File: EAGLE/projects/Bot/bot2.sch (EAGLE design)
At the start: 20 parts, among them IC1 7805T, U3 ARDUINO_SHIELDLABEL

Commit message: PCB Updates
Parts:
- removed S1: (no value), switch1:MS243
- added S2: (no value), switch2:MS243
- IC1: value 7805T -> (none); device linear:7805T -> linearMe:7905T
- LED1, LED2, LED3: device led:LED5MM -> ledMe:LED5MM
- U$1, U$2: value ULTRASONIC-HC-SR04#V -> ULTRASONIC-HC-SR04; device diy-modules:ULTRASONIC-HC-SR04#V -> diy-modules:ULTRASONIC-HC-SR04
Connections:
- removed net N$3: JP2.1, S1.P
- new net N$7: JP7.2, S2.P
- net 0: now also JP2.1, S2.S; no longer JP7.2, S1.S
- net PI_5V: now also LED1.A, LED2.A
- net PWR+: no longer LED1.A, LED2.A
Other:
- moved on the sheet: IC1
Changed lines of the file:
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@@
 </modules>
 <parts>
-<part name="IC1" library="linear" library_urn="urn:adsk.eagle:library:262" deviceset="78*" device="T" package3d_urn="urn:adsk.eagle:package:16414/1" technology="05"/>
+<part name="IC1" library="linearMe" deviceset="79*" device="T" package3d_urn="urn:adsk.eagle:package:16414/1" technology="05"/>
 <part name="JP2" library="pinhead" library_urn="urn:adsk.eagle:library:325" deviceset="PINHD-1X2" device="" package3d_urn="urn:adsk.eagle:package:22435/2"/>
 <part name="X_1" library="ngspice-simulation" library_urn="urn:adsk.eagle:library:527439" deviceset="GND" device=""/>
@@
 <part name="JP7" library="SparkFun" deviceset="M02" device="PTH4" value="SHIELD_PWR"/>
 <part name="U3" library="SparkFun" deviceset="ARDUINO_SHIELD" device="LABEL"/>
-<part name="X_7" library="ngspice-simulation" library_urn="urn:adsk.eagle:library:527439" deviceset="GND" device=""/>
 <part name="X_9" library="ngspice-simulation" library_urn="urn:adsk.eagle:library:527439" deviceset="GND" device=""/>
 <part name="X_8" library="ngspice-simulation" library_urn="urn:adsk.eagle:library:527439" deviceset="GND" device=""/>
-<part name="U$1" library="diy-modules" deviceset="ULTRASONIC-HC-SR04" device="#V"/>
-<part name="U$2" library="diy-modules" deviceset="ULTRASONIC-HC-SR04" device="#V"/>
-<part name="LED1" library="led" library_urn="urn:adsk.eagle:library:259" deviceset="LED" device="5MM" package3d_urn="urn:adsk.eagle:package:15799/2"/>
-<part name="LED2" library="led" library_urn="urn:adsk.eagle:library:259" deviceset="LED" device="5MM" package3d_urn="urn:adsk.eagle:package:15799/2"/>
+<part name="U$1" library="diy-modules" deviceset="ULTRASONIC-HC-SR04" device="" value="ULTRASONIC-HC-SR04"/>
+<part name="U$2" library="diy-modules" deviceset="ULTRASONIC-HC-SR04" device="" value="ULTRASONIC-HC-SR04"/>
+<part name="LED1" library="ledMe" deviceset="LED" device="5MM" package3d_urn="urn:adsk.eagle:package:15799/2"/>
+<part name="LED2" library="ledMe" deviceset="LED" device="5MM" package3d_urn="urn:adsk.eagle:package:15799/2"/>
 <part name="C1" library="rcl" library_urn="urn:adsk.eagle:library:334" deviceset="C-US" device="025-025X050" package3d_urn="urn:adsk.eagle:package:23629/2" value="330n"/>
 <part name="C2" library="rcl" library_urn="urn:adsk.eagle:library:334" deviceset="C-US" device="025-025X050" package3d_urn="urn:adsk.eagle:package:23629/2" value="100n"/>
 <part name="PI" library="raspberrypi_bastelstube_v13" deviceset="RASPI_BOARD_B+" device="_F" value="RASPI_BOARD_B+_F"/>
 <part name="KK1" library="heatsink" library_urn="urn:adsk.eagle:library:236" deviceset="SK129-PAD" device="" package3d_urn="urn:adsk.eagle:package:14199/1"/>
-<part name="LED3" library="led" library_urn="urn:adsk.eagle:library:259" deviceset="LED" device="5MM" package3d_urn="urn:adsk.eagle:package:15799/2"/>
+<part name="LED3" library="ledMe" deviceset="LED" device="5MM" package3d_urn="urn:adsk.eagle:package:15799/2"/>
 <part name="R6" library="resistor" library_urn="urn:adsk.eagle:library:348" deviceset="R-US_" device="0207/10" package3d_urn="urn:adsk.eagle:package:25939/1" value="100"/>
 <part name="X_3" library="ngspice-simulation" library_urn="urn:adsk.eagle:library:527439" deviceset="GND" device=""/>
-<part name="S1" library="switch1" deviceset="MS243" device="" package3d_urn="urn:adsk.eagle:package:27683/1"/>
+<part name="S2" library="switch2" deviceset="MS243" device="" package3d_urn="urn:adsk.eagle:package:27683/1"/>
+<part name="X_7" library="ngspice-simulation" library_urn="urn:adsk.eagle:library:527439" deviceset="GND" device=""/>
 </parts>
 <sheets>
@@
 <attribute name="VALUE" x="-39.37" y="-101.6" size="1.778" layer="96" rot="MR0"/>
 </instance>
-<instance part="X_7" gate="G$1" x="5.08" y="-78.74" smashed="yes"/>
 <instance part="X_9" gate="G$1" x="-33.02" y="-104.14" smashed="yes"/>
 <instance part="X_8" gate="G$1" x="-81.28" y="-99.06" smashed="yes"/>
@@
 </instance>
 <instance part="X_3" gate="G$1" x="-93.98" y="-50.8" smashed="yes"/>
-<instance part="S1" gate="1" x="-127" y="40.64" smashed="yes" rot="R180">
-<attribute name="NAME" x="-123.19" y="37.465" size="1.778" layer="95" rot="R270"/>
-<attribute name="VALUE" x="-125.73" y="37.465" size="1.778" layer="96" rot="R270"/>
-</instance>
+<instance part="S2" gate="1" x="7.62" y="-83.82" smashed="yes" rot="R180">
+<attribute name="NAME" x="11.43" y="-86.995" size="1.778" layer="95" rot="R270"/>
+<attribute name="VALUE" x="8.89" y="-86.995" size="1.778" layer="96" rot="R270"/>
+</instance>
+<instance part="X_7" gate="G$1" x="5.08" y="-96.52" smashed="yes"/>
 </instances>
 <busses>
@@
 <label x="-119.38" y="53.34" size="1.778" layer="95"/>
 <pinref part="C1" gate="G$1" pin="1"/>
-<wire x1="-116.84" y1="53.34" x2="-106.68" y2="53.34" width="0.1524" layer="91"/>
+<wire x1="-116.84" y1="53.34" x2="-106.68" y2="50.8" width="0.1524" layer="91"/>
 <junction x="-116.84" y="53.34"/>
-</segment>
-<segment>
-<wire x1="-104.14" y1="-5.08" x2="-121.92" y2="-5.08" width="0.1524" layer="91"/>
-<label x="-121.92" y="-5.08" size="1.778" layer="95"/>
-<pinref part="LED2" gate="G$1" pin="A"/>
-<wire x1="-104.14" y1="12.7" x2="-121.92" y2="12.7" width="0.1524" layer="91"/>
-<label x="-129.54" y="12.7" size="1.778" layer="95"/>
-<pinref part="LED1" gate="G$1" pin="A"/>
-<wire x1="-121.92" y1="-5.08" x2="-121.92" y2="12.7" width="0.1524" layer="91"/>
-<wire x1="-121.92" y1="12.7" x2="-129.54" y2="12.7" width="0.1524" layer="91"/>
-<junction x="-121.92" y="12.7"/>
 </segment>
 <segment>
@@
 <pinref part="X_1" gate="G$1" pin="0"/>
 <wire x1="-116.84" y1="45.72" x2="-109.22" y2="45.72" width="0.1524" layer="91"/>
-<wire x1="-109.22" y1="45.72" x2="-96.52" y2="45.72" width="0.1524" layer="91"/>
+<wire x1="-109.22" y1="45.72" x2="-96.52" y2="58.42" width="0.1524" layer="91"/>
 <wire x1="-109.22" y1="38.1" x2="-109.22" y2="45.72" width="0.1524" layer="91"/>
 <junction x="-109.22" y="45.72"/>
 <pinref part="C1" gate="G$1" pin="2"/>
 <pinref part="C2" gate="G$1" pin="2"/>
-<wire x1="-83.82" y1="45.72" x2="-96.52" y2="45.72" width="0.1524" layer="91"/>
-<junction x="-96.52" y="45.72"/>
-<wire x1="-116.84" y1="45.72" x2="-116.84" y2="33.02" width="0.1524" layer="91"/>
+<wire x1="-83.82" y1="45.72" x2="-96.52" y2="58.42" width="0.1524" layer="91"/>
+<junction x="-96.52" y="58.42"/>
+<wire x1="-129.54" y1="30.48" x2="-116.84" y2="30.48" width="0.1524" layer="91"/>
+<wire x1="-116.84" y1="30.48" x2="-116.84" y2="45.72" width="0.1524" layer="91"/>
 <junction x="-116.84" y="45.72"/>
-<pinref part="S1" gate="1" pin="S"/>
-<wire x1="-116.84" y1="33.02" x2="-129.54" y2="33.02" width="0.1524" layer="91"/>
-<wire x1="-129.54" y1="33.02" x2="-129.54" y2="35.56" width="0.1524" layer="91"/>
+<pinref part="JP2" gate="G$1" pin="1"/>
+<wire x1="-129.54" y1="50.8" x2="-129.54" y2="30.48" width="0.1524" layer="91"/>
 </segment>
 <segment>
@@
 <pinref part="R5" gate="G$1" pin="1"/>
 <wire x1="-129.54" y1="-27.94" x2="-129.54" y2="-25.4" width="0.1524" layer="91"/>
-</segment>
-<segment>
-<pinref part="JP7" gate="G$1" pin="2"/>
-<pinref part="X_7" gate="G$1" pin="0"/>
-<wire x1="-15.24" y1="-76.2" x2="5.08" y2="-76.2" width="0.1524" layer="91"/>
-<wire x1="5.08" y1="-76.2" x2="5.08" y2="-78.74" width="0.1524" layer="91"/>
 </segment>
 <segment>
@@
 <pinref part="R6" gate="G$1" pin="1"/>
 <wire x1="-93.98" y1="-50.8" x2="-93.98" y2="-45.72" width="0.1524" layer="91"/>
+</segment>
+<segment>
+<pinref part="S2" gate="1" pin="S"/>
+<pinref part="X_7" gate="G$1" pin="0"/>
+<wire x1="5.08" y1="-88.9" x2="5.08" y2="-96.52" width="0.1524" layer="91"/>
 </segment>
 </net>
@@
 <segment>
 <pinref part="IC1" gate="A1" pin="VO"/>
-<wire x1="-86.36" y1="53.34" x2="-83.82" y2="53.34" width="0.1524" layer="91"/>
+<wire x1="-86.36" y1="50.8" x2="-83.82" y2="53.34" width="0.1524" layer="91"/>
 <label x="-78.74" y="53.34" size="1.778" layer="95"/>
 <pinref part="C2" gate="G$1" pin="1"/>
 <junction x="-83.82" y="53.34"/>
 <wire x1="-83.82" y1="53.34" x2="-71.12" y2="53.34" width="0.1524" layer="91"/>
+</segment>
+<segment>
+<wire x1="-104.14" y1="-5.08" x2="-121.92" y2="-5.08" width="0.1524" layer="91"/>
+<label x="-121.92" y="-5.08" size="1.778" layer="95"/>
+<pinref part="LED2" gate="G$1" pin="A"/>
+<wire x1="-104.14" y1="12.7" x2="-121.92" y2="12.7" width="0.1524" layer="91"/>
+<label x="-129.54" y="12.7" size="1.778" layer="95"/>
+<pinref part="LED1" gate="G$1" pin="A"/>
+<wire x1="-121.92" y1="-5.08" x2="-121.92" y2="12.7" width="0.1524" layer="91"/>
+<wire x1="-121.92" y1="12.7" x2="-129.54" y2="12.7" width="0.1524" layer="91"/>
+<junction x="-121.92" y="12.7"/>
 </segment>
 </net>
@@
 </segment>
 </net>
-<net name="N$3" class="0">
-<segment>
-<pinref part="S1" gate="1" pin="P"/>
-<pinref part="JP2" gate="G$1" pin="1"/>
-<wire x1="-129.54" y1="45.72" x2="-129.54" y2="50.8" width="0.1524" layer="91"/>
-</segment>
-</net>
+<net name="N$7" class="0">
+<segment>
+<pinref part="JP7" gate="G$1" pin="2"/>
+<wire x1="-15.24" y1="-76.2" x2="5.08" y2="-76.2" width="0.1524" layer="91"/>
+<wire x1="5.08" y1="-76.2" x2="5.08" y2="-78.74" width="0.1524" layer="91"/>
+<pinref part="S2" gate="1" pin="P"/>
+</segment>
+</net>

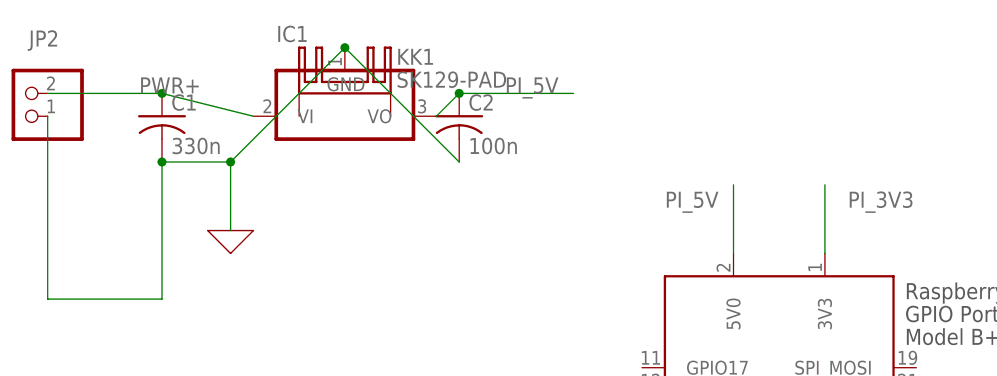
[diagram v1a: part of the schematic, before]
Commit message: Fixed voltage reg on Eagle
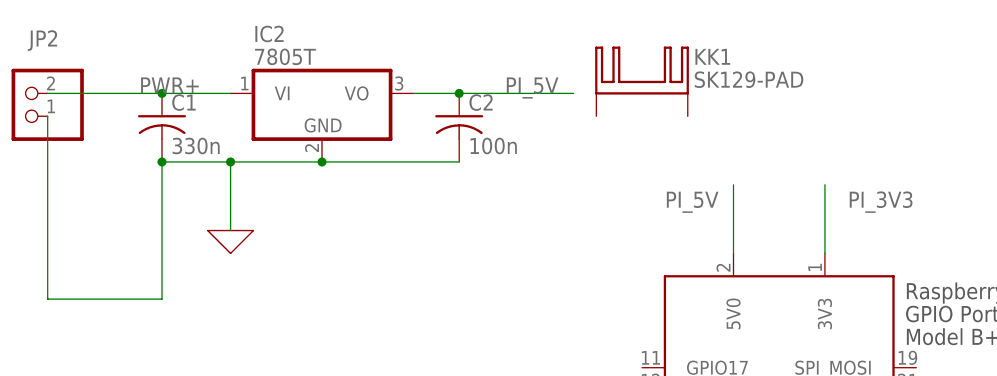
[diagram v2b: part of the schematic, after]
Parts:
- removed IC1: (no value), linearMe:7905T
- added IC2: 7805T, linear:7805T
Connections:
- net 0: now also IC2.GND; no longer IC1.GND
- net PI_5V: now also IC2.VO; no longer IC1.VO
- net PWR+: now also IC2.VI; no longer IC1.VI
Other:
- moved on the sheet: KK1
